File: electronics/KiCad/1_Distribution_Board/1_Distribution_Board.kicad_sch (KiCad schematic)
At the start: 12 parts, among them J1 Conn_02x08_Odd_Even, J2 Conn_01x10, J3 Conn_01x06, Q1 DMG2305UX, SW1 SW_Push

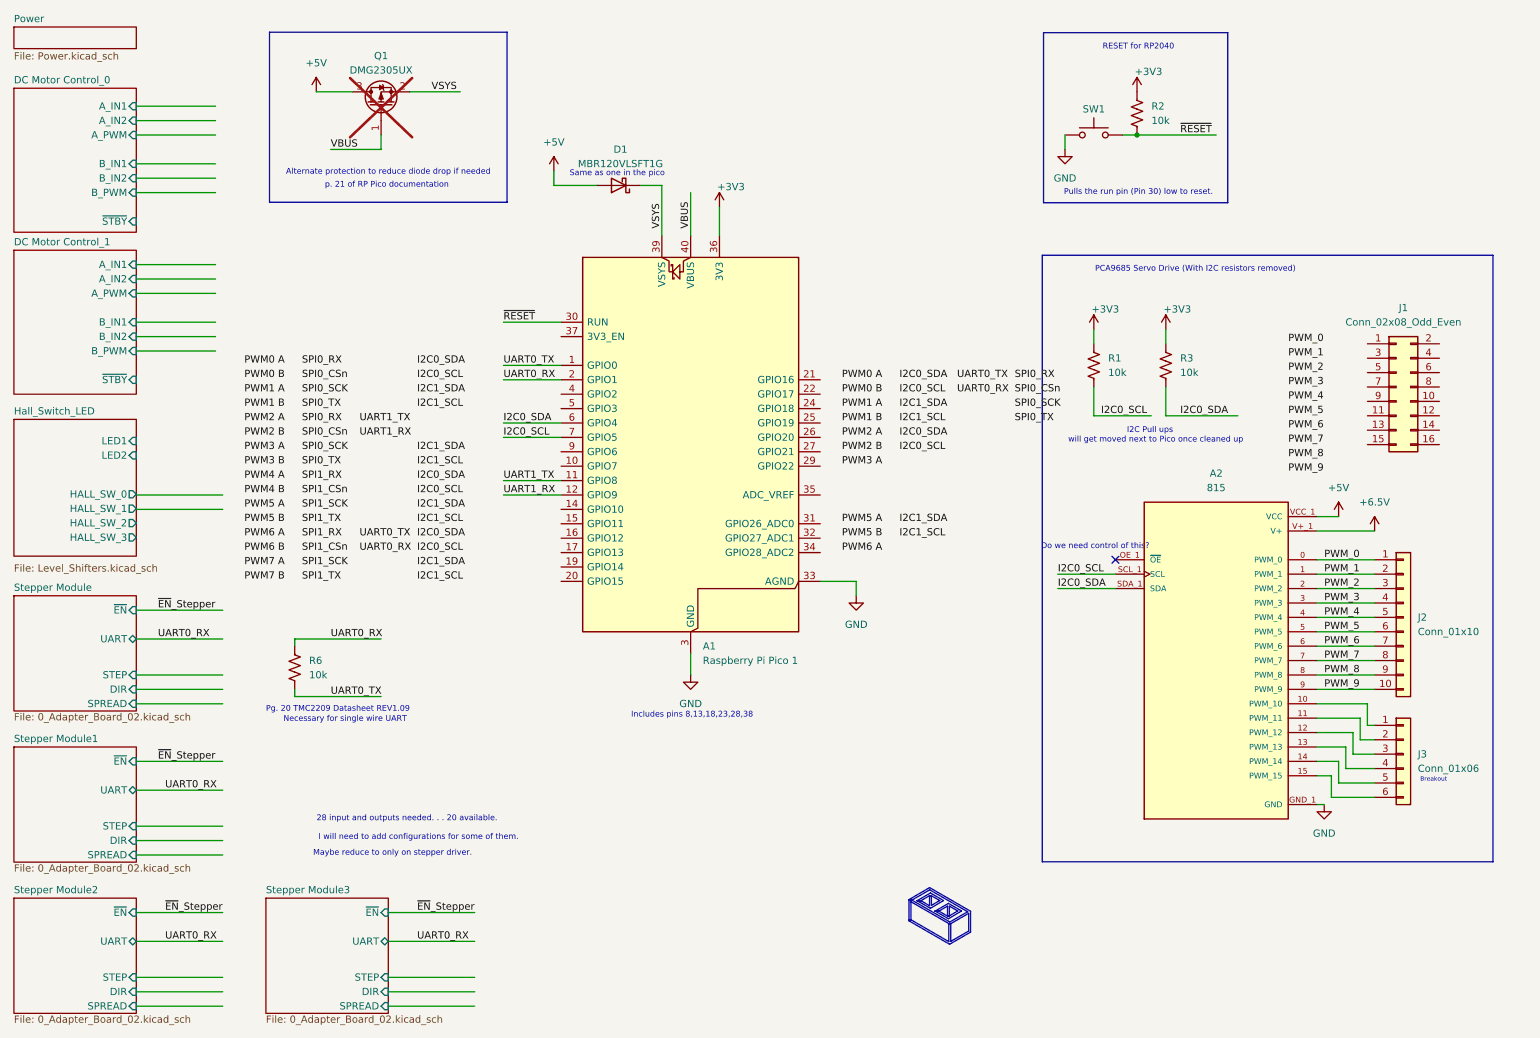
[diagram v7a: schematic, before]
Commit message: Updated Schematic naming, PCB work
Updated Schematic naming for sub-sheets to get rid of untitled and adapter board ones. ADD - 815 sub-sheet for cleaner printable schematic.

PCB:

Started moving modules to socket headers for easy of prototyping.
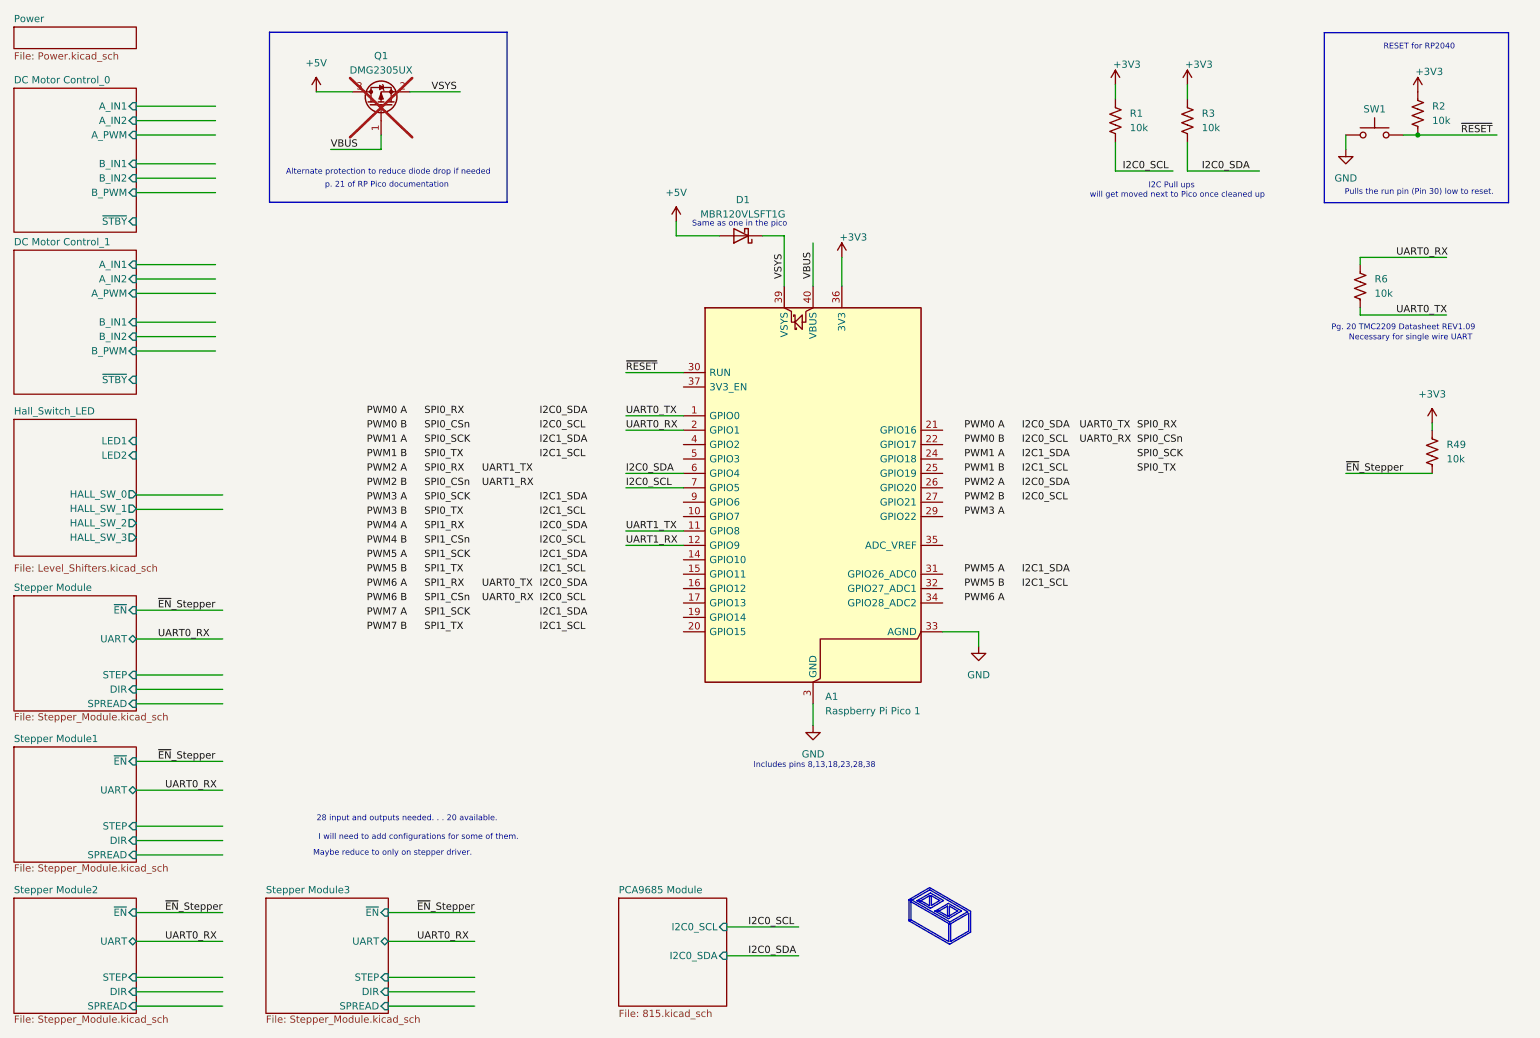
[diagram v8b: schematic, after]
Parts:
- removed A2: 815, 815:MODULE_815, symbol 815:815
- removed J1: Conn_02x08_Odd_Even, symbol Connector_Generic:Conn_02x08_Odd_Even
- removed J2: Conn_01x10, Connector_JST:JST_XA_B10B-XASK-1-A_1x10_P2.50mm_Vertical, symbol Connector_Generic:Conn_01x10
- removed J3: Conn_01x06, Connector_PinHeader_2.54mm:PinHeader_1x06_P2.54mm_Vertical, symbol Connector_Generic:Conn_01x06
- added R49: 10k, Resistor_SMD:R_0805_2012Metric_Pad1.20x1.40mm_HandSolder, symbol Device:R_US
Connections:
- net +3V3: now also R49.1
- net ~{EN}_Stepper: now also R49.2
- no-connect marks 1 -> 0
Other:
- added sheet PCA9685 Module (815.kicad_sch)
- sheet DC Motor Control_0: file untitled.kicad_sch -> DC_Motor_Controller.kicad_sch
- sheet DC Motor Control_1: file untitled.kicad_sch -> DC_Motor_Controller.kicad_sch
- sheet Stepper Module: file 0_Adapter_Board_02.kicad_sch -> Stepper_Module.kicad_sch
- sheet Stepper Module1: file 0_Adapter_Board_02.kicad_sch -> Stepper_Module.kicad_sch
- sheet Stepper Module2: file 0_Adapter_Board_02.kicad_sch -> Stepper_Module.kicad_sch
- sheet Stepper Module3: file 0_Adapter_Board_02.kicad_sch -> Stepper_Module.kicad_sch
- note removed: "Breakout"
- note removed: "Do we need control of this?"
- note removed: "PCA9685 Servo Drive (With I2C resistors removed)"
- moved on the sheet: A1, D1, R1, R2, R3, R6, SW1
